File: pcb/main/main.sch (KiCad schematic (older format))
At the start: 41 parts, among them J1 USB_B_Micro, J2 Conn_01x12, J3 ISP, J4 Conn_01x12, Q1 DMP3099L, SW1 SW_Push, U1 CH340G, U2 TLV70033, U3 ATmega328P-AU, U4 RFM95W-915S2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

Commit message: Added custom symbols lib
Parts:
- Q1: symbol Transistor_FET:DMP3099L -> custom:DMP3099L
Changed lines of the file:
@@
 $EndComp
 $Comp
-L power:VBAT #PWR07
+L custom:VBAT #PWR07
 U 1 1 6081E169
 P 7150 5200
@@
 	7150 5600 7600 5600
 $Comp
-L power:VBAT #PWR022
+L custom:VBAT #PWR022
 U 1 1 60B7C463
 P 10100 4950
@@
 	2700 6700 2850 6700
 $Comp
-L Transistor_FET:DMP3099L Q1
+L custom:DMP3099L Q1
 U 1 1 607A6C73
 P 7600 5350

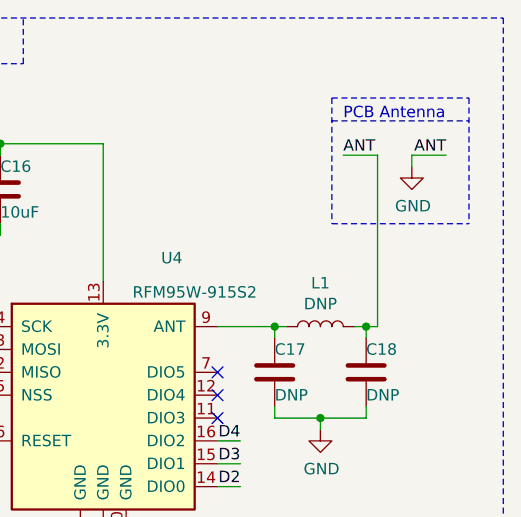
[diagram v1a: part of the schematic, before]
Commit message: Added antenna footprint
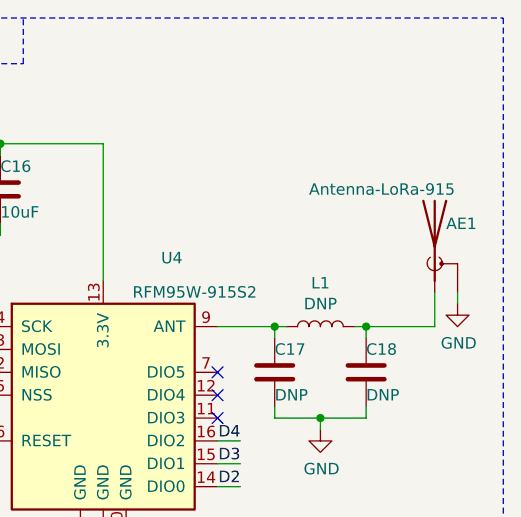
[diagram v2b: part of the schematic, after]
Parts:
- added AE1: Antenna-LoRa-915, symbol Device:Antenna_Shield
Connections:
- net GND: now also AE1.2 (Shield); no longer C18.1, L1.2
- new net: AE1.1 (A), C18.1, L1.2
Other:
- note removed: "PCB Antenna"
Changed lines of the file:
@@
 L power:GND #PWR040
 U 1 1 6066AC55
-P 10400 1750
-F 0 "#PWR040" H 10400 1500 50  0001 C CNN
-F 1 "GND" H 10405 1577 50  0000 C CNN
-F 2 "" H 10400 1750 50  0001 C CNN
-F 3 "" H 10400 1750 50  0001 C CNN
-	1    10400 1750
+P 10600 2350
+F 0 "#PWR040" H 10600 2100 50  0001 C CNN
+F 1 "GND" H 10605 2177 50  0000 C CNN
+F 2 "" H 10600 2350 50  0001 C CNN
+F 3 "" H 10600 2350 50  0001 C CNN
+	1    10600 2350
 	1    0    0    -1
 $EndComp
@@
 Text Label 9650 2950 2    50   ~ 0
 D4
-Text Label 10550 1700 2    50   ~ 0
-ANT
-Text Label 10100 1700 0    50   ~ 0
-ANT
-Wire Wire Line
-	10100 1700 10250 1700
-Wire Wire Line
-	10400 1700 10550 1700
-Wire Wire Line
-	10200 2450 10250 2450
+$Comp
+L Device:Antenna_Shield AE1
+U 1 1 607C825D
+P 10500 2100
+F 0 "AE1" H 10550 2200 50  0000 L CNN
+F 1 "Antenna-LoRa-915" H 9950 2350 50  0000 L CNN
+F 2 "" H 10500 2200 50  0001 C CNN
+F 3 "~" H 10500 2200 50  0001 C CNN
+	1    10500 2100
+	1    0    0    -1
+$EndComp
+Wire Wire Line
+	10600 2350 10600 2300
+Wire Wire Line
+	10500 2300 10500 2450
+Wire Wire Line
+	10500 2450 10200 2450
 Connection ~ 10200 2450
-Wire Wire Line
-	10400 1750 10400 1700
-Wire Wire Line
-	10250 1700 10250 2450
-Text Notes 10100 1550 0    50   ~ 0
-PCB Antenna
-Wire Notes Line
-	10050 1450 10050 2000
-Wire Notes Line
-	10650 1450 10650 2000
-Wire Notes Line
-	10050 2000 10650 2000
-Wire Notes Line
-	10050 1450 10650 1450
-Wire Notes Line
-	10050 1550 10650 1550
 $EndSCHEMATC

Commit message: Fix previous commit
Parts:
- AE1: footprint (none) -> custom_lib:antenna-lora-915
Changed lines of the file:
@@
 F 0 "AE1" H 10550 2200 50  0000 L CNN
 F 1 "Antenna-LoRa-915" H 9950 2350 50  0000 L CNN
-F 2 "" H 10500 2200 50  0001 C CNN
+F 2 "custom_lib:antenna-lora-915" H 10500 2200 50  0001 C CNN
 F 3 "~" H 10500 2200 50  0001 C CNN
 	1    10500 2100

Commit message: Fix - Correcciones solicitadas
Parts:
- removed Y2: 32.768Hz, Crystal:Crystal_SMD_Abracon_ABS25-4Pin_8.0x3.8mm, symbol Device:Crystal
- added Y2: 32.768 Hz, Crystal:Crystal_SMD_Abracon_ABS25-4Pin_8.0x3.8mm, symbol Device:Crystal_GND23
- AE1: footprint custom_lib:antenna-lora-915 -> custom:antenna-lora-915
- BT1: Digikey PN (none) -> BH-18650-PC-ND
- D1: Digikey PN (none) -> MBR0520LT1GOSCT-ND
- J1: Digikey PN (none) -> WM17141CT-ND
- Q1: Digikey PN (none) -> DMP3099L-7DICT-ND
- U2: Digikey PN (none) -> 296-25276-1-ND
- U3: Digikey PN (none) -> ATMEGA328P-AU-ND
- Y1: footprint Crystal:Crystal_SMD_HC49-SD_HandSoldering -> Crystal:Crystal_SMD_HC49-SD; Digikey PN (none) -> 1923-1541-1-ND
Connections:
- net A0: now also J4.3 (Pin_3); no longer J4.9 (Pin_9)
- net A1: now also J4.4 (Pin_4); no longer J4.8 (Pin_8)
- net A2: now also J4.5 (Pin_5); no longer J4.7 (Pin_7)
- net A4: now also J4.7 (Pin_7); no longer J4.5 (Pin_5)
- net A5: now also J4.8 (Pin_8); no longer J4.4 (Pin_4)
- net A6: now also J4.9 (Pin_9); no longer J4.3 (Pin_3)
- net D2: now also J2.10 (Pin_10); no longer J2.5 (Pin_5)
- net D3: now also J2.9 (Pin_9); no longer J2.6 (Pin_6)
- net D4: now also J2.8 (Pin_8); no longer J2.7 (Pin_7)
- net D5: now also J2.7 (Pin_7); no longer J2.8 (Pin_8)
- net D6: now also J2.6 (Pin_6); no longer J2.9 (Pin_9)
- net D7: now also J2.5 (Pin_5); no longer J2.10 (Pin_10)
- net GND: now also J4.12 (Pin_12), Y2.2, Y2.3; no longer J2.2 (Pin_2)
- net MISO: now also J2.3 (Pin_3); no longer J2.12 (Pin_12)
- net MOSI: now also J2.4 (Pin_4); no longer J2.11 (Pin_11)
- net RX: now also J2.12 (Pin_12); no longer J2.3 (Pin_3)
- net RXD: now also J2.11 (Pin_11); no longer J2.4 (Pin_4)
- net SCK: now also J2.2 (Pin_2); no longer J4.12 (Pin_12)
- net at C9.1, U3.7 (XTAL1/PB6): now also Y2.4
- net at C8.1, U3.8 (XTAL2/PB7): now also Y2.1
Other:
- note added: "Battery holder\n 18650"
- moved on the sheet: BT1, R4, R5

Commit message: PCB added
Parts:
- added FID1, FID2, FID3, FID4: Fiducial, Fiducial:Fiducial_0.5mm_Mask1.5mm, symbol Mechanical:Fiducial
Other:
- note added: "Fiducial"
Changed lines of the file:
@@
 Text Notes 10000 4850 0    50   ~ 0
 Battery holder\n    18650
+$Comp
+L Mechanical:Fiducial FID1
+U 1 1 60A03FB7
+P 5250 4900
+F 0 "FID1" H 5335 4946 50  0000 L CNN
+F 1 "Fiducial" H 5335 4855 50  0000 L CNN
+F 2 "Fiducial:Fiducial_0.5mm_Mask1.5mm" H 5250 4900 50  0001 C CNN
+F 3 "~" H 5250 4900 50  0001 C CNN
+	1    5250 4900
+	1    0    0    -1
+$EndComp
+$Comp
+L Mechanical:Fiducial FID2
+U 1 1 60A05225
+P 5250 5100
+F 0 "FID2" H 5335 5146 50  0000 L CNN
+F 1 "Fiducial" H 5335 5055 50  0000 L CNN
+F 2 "Fiducial:Fiducial_0.5mm_Mask1.5mm" H 5250 5100 50  0001 C CNN
+F 3 "~" H 5250 5100 50  0001 C CNN
+	1    5250 5100
+	1    0    0    -1
+$EndComp
+$Comp
+L Mechanical:Fiducial FID3
+U 1 1 60A05624
+P 5250 5300
+F 0 "FID3" H 5335 5346 50  0000 L CNN
+F 1 "Fiducial" H 5335 5255 50  0000 L CNN
+F 2 "Fiducial:Fiducial_0.5mm_Mask1.5mm" H 5250 5300 50  0001 C CNN
+F 3 "~" H 5250 5300 50  0001 C CNN
+	1    5250 5300
+	1    0    0    -1
+$EndComp
+$Comp
+L Mechanical:Fiducial FID4
+U 1 1 60A05ABC
+P 5250 5500
+F 0 "FID4" H 5335 5546 50  0000 L CNN
+F 1 "Fiducial" H 5335 5455 50  0000 L CNN
+F 2 "Fiducial:Fiducial_0.5mm_Mask1.5mm" H 5250 5500 50  0001 C CNN
+F 3 "~" H 5250 5500 50  0001 C CNN
+	1    5250 5500
+	1    0    0    -1
+$EndComp
+Wire Notes Line
+	5850 4600 5000 4600
+Text Notes 5050 4700 0    50   ~ 0
+Fiducial
+Wire Notes Line
+	5000 4750 5400 4750
+Wire Notes Line
+	5400 4750 5400 4600
+Wire Notes Line
+	5000 5650 5850 5650
+Wire Notes Line
+	5850 4600 5850 5650
+Wire Notes Line
+	5000 4600 5000 5650
 $EndSCHEMATC

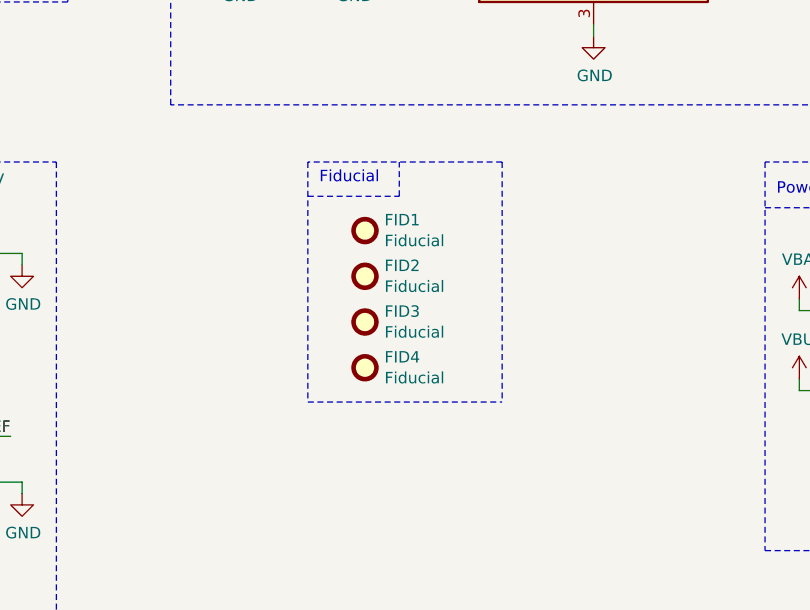
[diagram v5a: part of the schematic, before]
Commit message: Fix fiducials and annotations
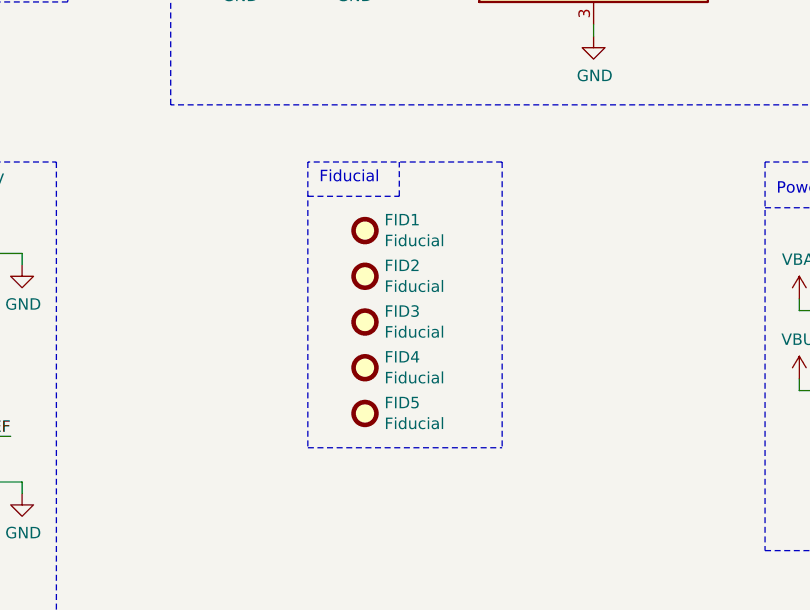
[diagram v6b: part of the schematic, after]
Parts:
- added FID5: Fiducial, Fiducial:Fiducial_0.5mm_Mask1.5mm, symbol Mechanical:Fiducial
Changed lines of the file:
@@
 	5400 4750 5400 4600
 Wire Notes Line
-	5000 5650 5850 5650
+	5000 5850 5850 5850
+$Comp
+L Mechanical:Fiducial FID5
+U 1 1 60860524
+P 5250 5700
+F 0 "FID5" H 5335 5746 50  0000 L CNN
+F 1 "Fiducial" H 5335 5655 50  0000 L CNN
+F 2 "Fiducial:Fiducial_0.5mm_Mask1.5mm" H 5250 5700 50  0001 C CNN
+F 3 "~" H 5250 5700 50  0001 C CNN
+	1    5250 5700
+	1    0    0    -1
+$EndComp
 Wire Notes Line
-	5850 4600 5850 5650
+	5850 4600 5850 5850
 Wire Notes Line
-	5000 4600 5000 5650
+	5000 4600 5000 5850
 $EndSCHEMATC
